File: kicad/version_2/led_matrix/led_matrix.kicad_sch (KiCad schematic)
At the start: 82 parts, among them Q1 IRF540N, Q2 IRF540N, Q3 IRF540N, Q4 IRF540N, Q5 IRF540N, Q6 IRF540N, Q7 IRF540N, Q9 IRF540N, SW1 SW_DIP_x01

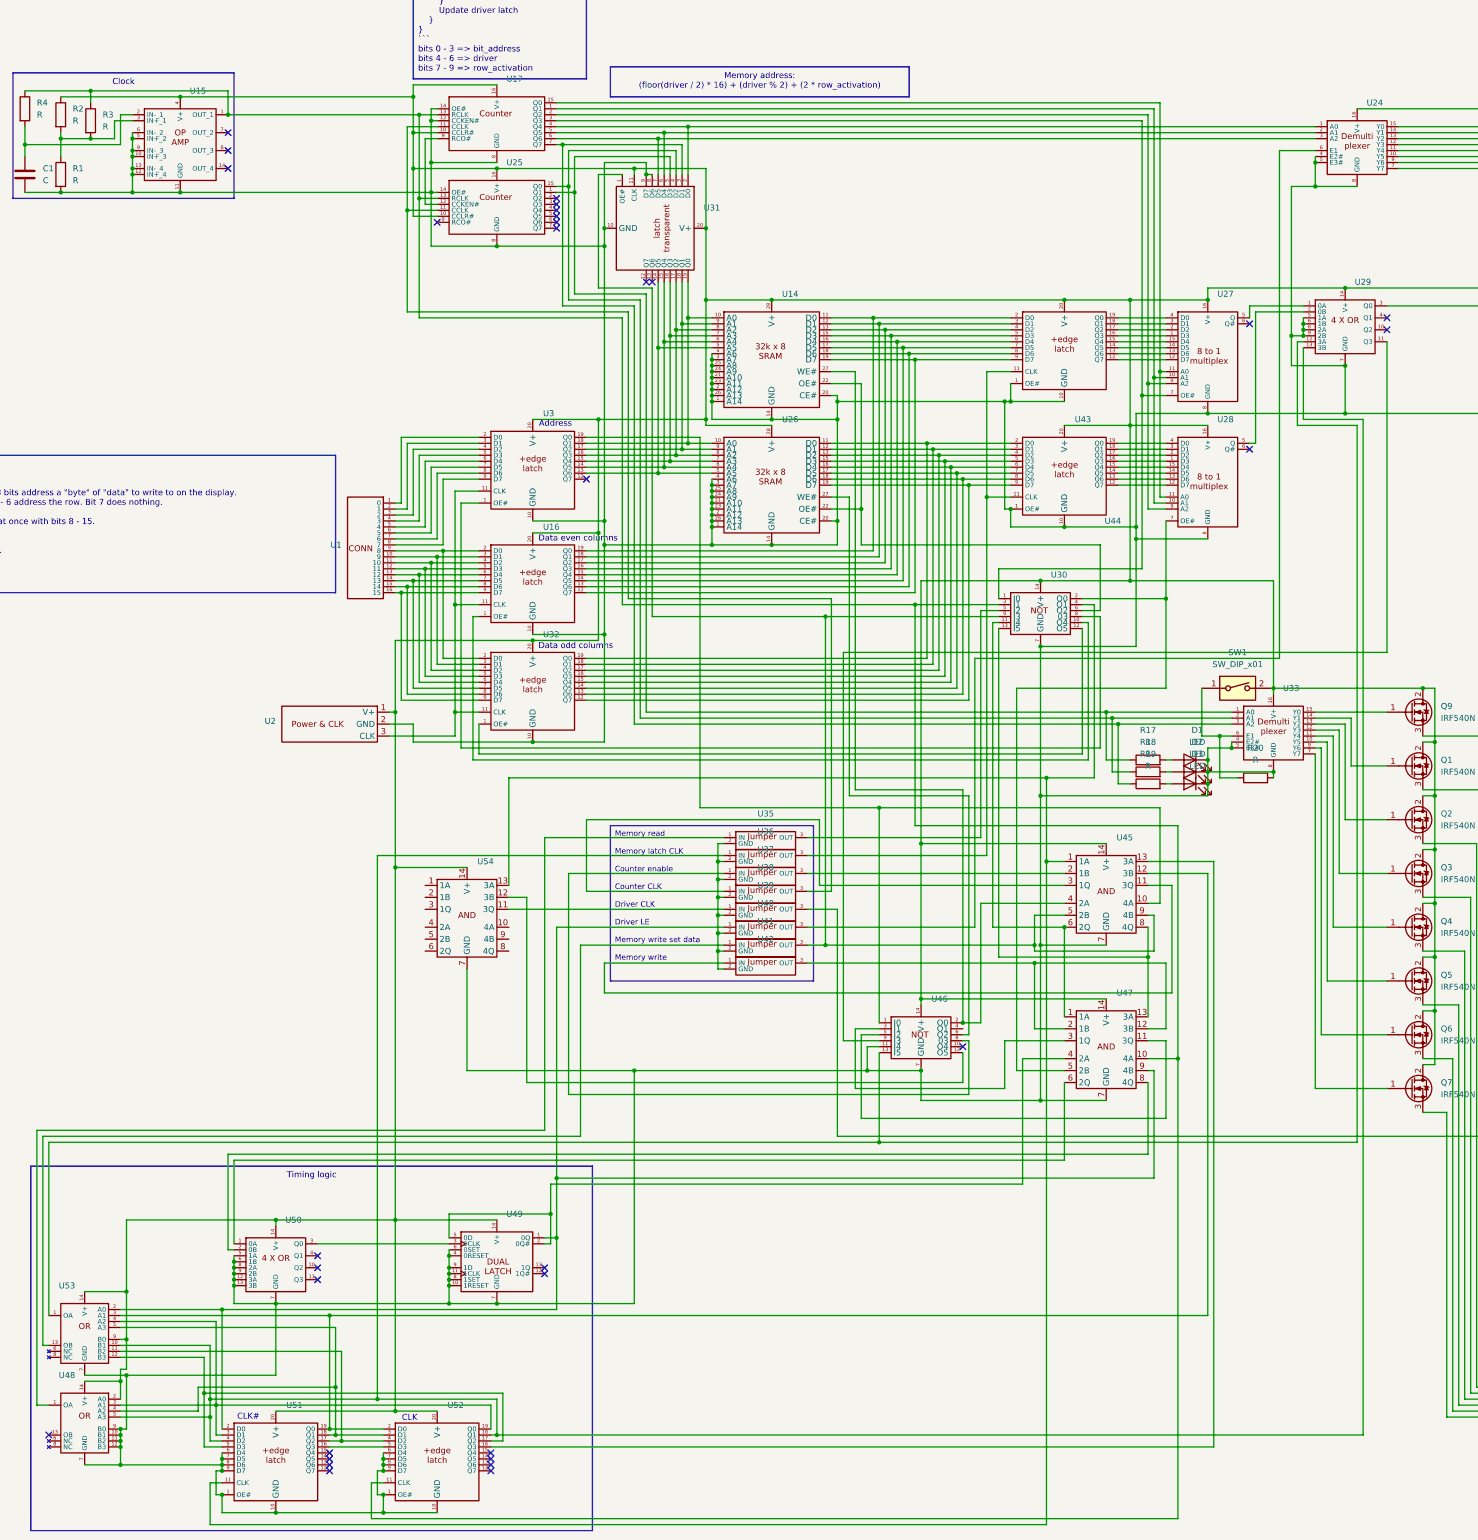
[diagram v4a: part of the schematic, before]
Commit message: LED matrix PCB done
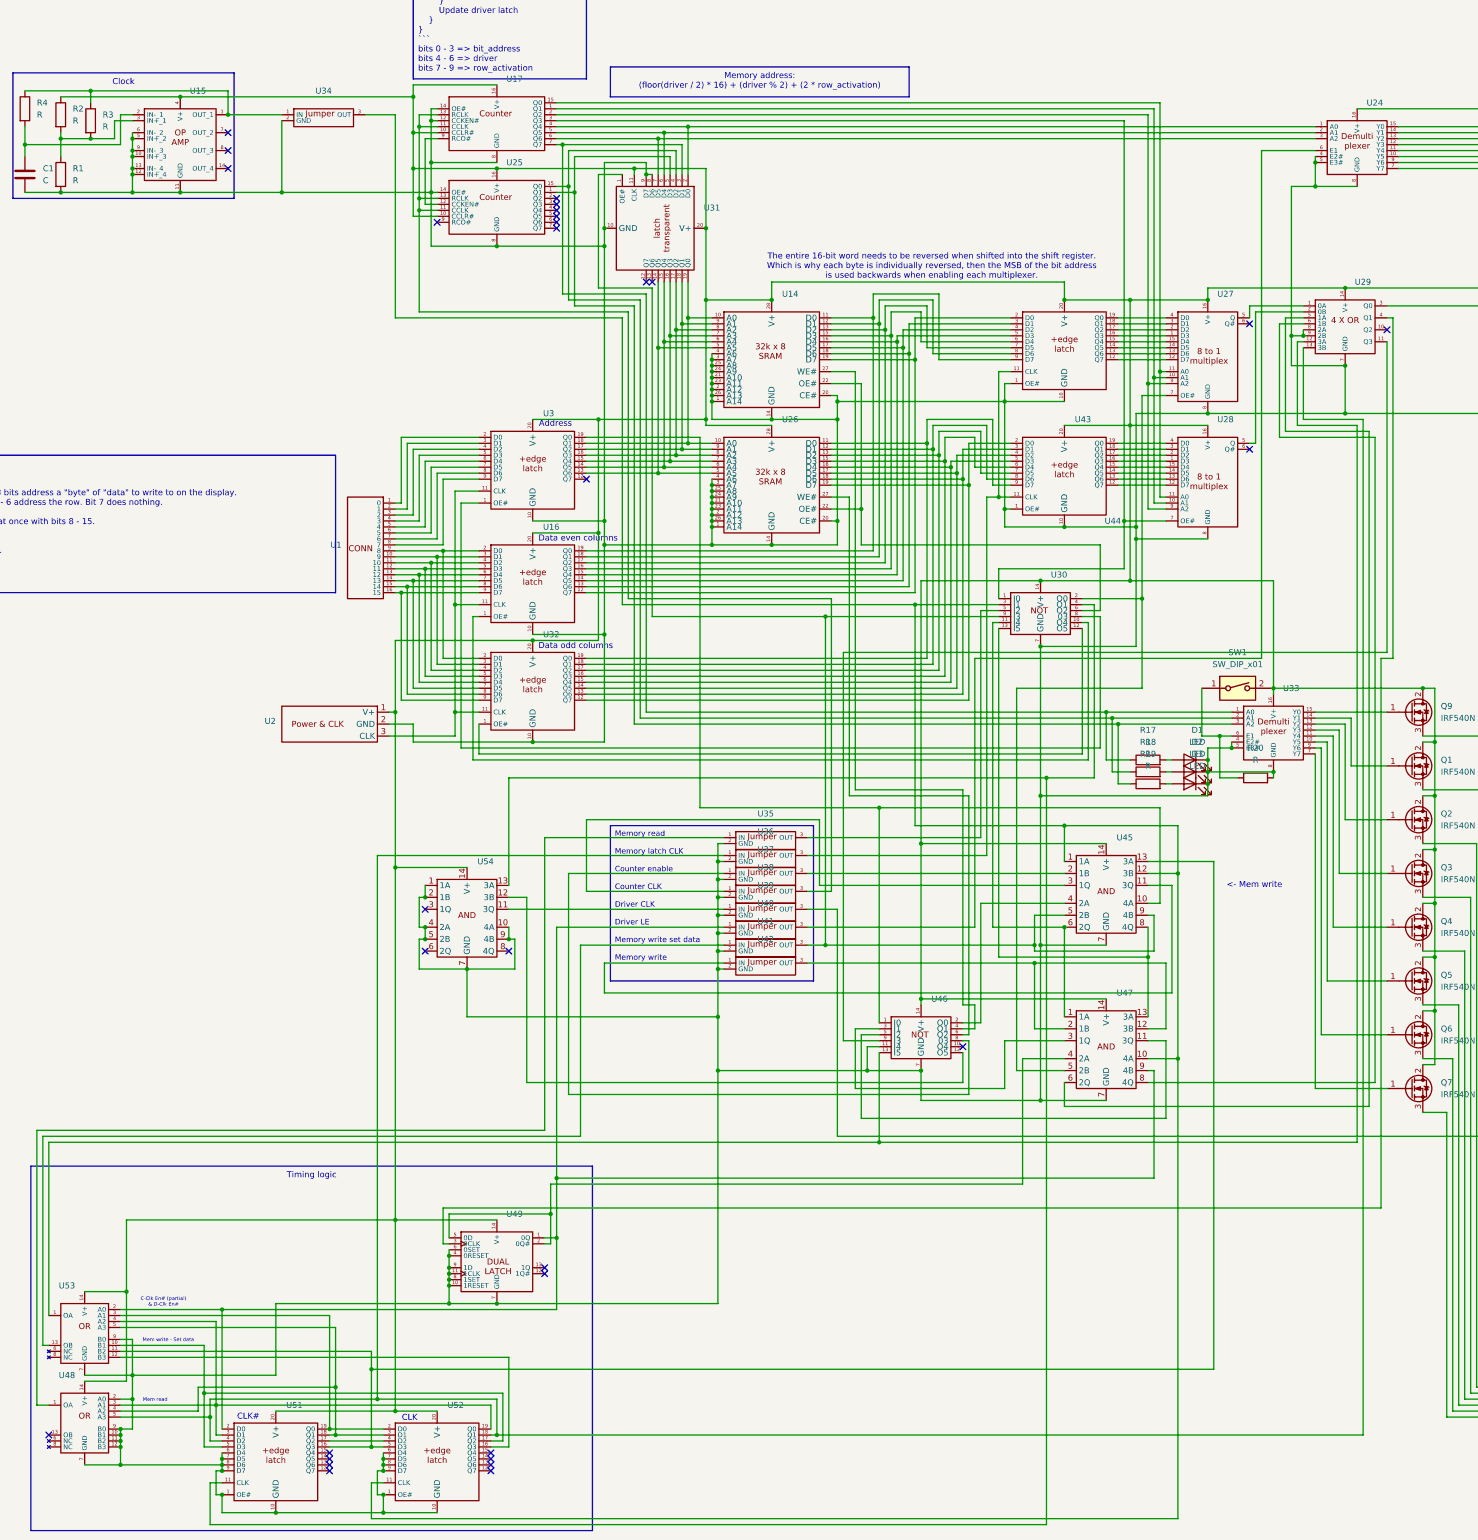
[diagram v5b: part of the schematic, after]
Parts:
- removed U50: ~, Package_DIP:DIP-14_W7.62mm, symbol custom_symbol_lib:quad_OR
- added U34: ~, custom_footprint_library:jumper, symbol custom_symbol_lib:jumper
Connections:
- net at U29.13 (3B), U36.1 (IN), U48.5 (A3)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: no longer U53.10 (B1)
- net at U51.17 (Q2), U52.4 (D2): no longer U53.11 (B2)
- net at U51.5 (D3), U52.17 (Q2): now also U53.10 (B1); no longer U53.12 (B3)
- net at Q1.2 (D), Q2.2 (D), Q3.2 (D)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: no longer U48.2 (A0), U53.9 (B0)
- net at U51.19 (Q0), U52.2 (D0), U53.3 (A1): no longer U45.12 (3B)
- net at C1.2, D1.1 (K), D2.1 (K)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: now also U35.2 (GND), U36.2 (GND), U37.2 (GND), U38.2 (GND), U39.2 (GND), U40.2 (GND), U41.2 (GND), U42.2 (GND), U48.2 (A0), U53.9 (B0), U54.1 (1A), U54.10 (4A), U54.2 (1B), U54.4 (2A), U54.5 (2B), U54.9 (4B), U34.2 (GND); no longer U29.5 (1A), U29.6 (1B)
- net at U17.3 (Q3), U30.1 (I0): now also U28.7 (OE#); no longer U27.7 (OE#)
- net at U30.2 (O0), U47.5 (2B): now also U27.7 (OE#); no longer U28.7 (OE#)
- net at U30.4 (O1), U51.11 (CLK), U54.13 (3A): no longer U45.1 (1A)
- net at U49.3 (0CLK): now also U29.4 (Q1)
- net at U45.13 (3A): now also U51.16 (Q3), U52.5 (D3), U53.11 (B2); no longer U52.16 (Q3)
- net at U45.4 (2A), U46.2 (O0): no longer U14.27 (WE#)
- net at U17.11 (CCLK), U25.11 (CCLK), U38.3 (OUT): now also U17.13 (RCLK), U25.13 (RCLK)
- net at U17.7 (Q7), U31.3 (D1): now also R17.1, U33.1 (A0); no longer R19.1, U33.3 (A2)
- net at U47.6 (2Q): now also U29.5 (1A)
- net at U47.8 (4Q): now also U29.6 (1B)
- net at U14.19 (D7), U16.12 (Q7): now also U44.2 (D0); no longer U44.9 (D7)
- net at U14.18 (D6), U16.13 (Q6): now also U44.3 (D1); no longer U44.8 (D6)
- net at U14.17 (D5), U16.14 (Q5): now also U44.4 (D2); no longer U44.7 (D5)
- net at U14.16 (D4), U16.15 (Q4): now also U44.5 (D3); no longer U44.6 (D4)
- net at U14.15 (D3), U16.16 (Q3): now also U44.6 (D4); no longer U44.5 (D3)
- net at U14.13 (D2), U16.17 (Q2): now also U44.7 (D5); no longer U44.4 (D2)
- net at U14.12 (D1), U16.18 (Q1): now also U44.8 (D6); no longer U44.3 (D1)
- net at U14.11 (D0), U16.19 (Q0): now also U44.9 (D7); no longer U44.2 (D0)
- net at U25.1 (Q1), U31.5 (D3): now also R19.1, U33.3 (A2); no longer R17.1, U33.1 (A0)
- net at U26.11 (D0), U32.19 (Q0): now also U43.9 (D7); no longer U43.2 (D0)
- net at U26.12 (D1), U32.18 (Q1): now also U43.8 (D6); no longer U43.3 (D1)
- net at U26.13 (D2), U32.17 (Q2): now also U43.7 (D5); no longer U43.4 (D2)
- net at U26.15 (D3), U32.16 (Q3): now also U43.6 (D4); no longer U43.5 (D3)
- net at U26.16 (D4), U32.15 (Q4): now also U43.5 (D3); no longer U43.6 (D4)
- net at U26.17 (D5), U32.14 (Q5): now also U43.4 (D2); no longer U43.7 (D5)
- net at U26.18 (D6), U32.13 (Q6): now also U43.3 (D1); no longer U43.8 (D6)
- net at U26.19 (D7), U32.12 (Q7): now also U43.2 (D0); no longer U43.9 (D7)
- net at U46.4 (O1): now also U14.27 (WE#)
- new net: U52.16 (Q3), U53.12 (B3)
- new net: U30.3 (I1), U34.3 (OUT), U45.1 (1A), U45.12 (3B), U47.10 (4A), U52.11 (CLK)
- new net: R3.1, R4.1, U15.1 (OUT_1), U34.1 (IN)
- no-connect marks 40 -> 39
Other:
- note added: "<- Mem write"
- note added: "C-Clk En# (partial) & D-Clk En#"
- note added: "Mem read"
- note added: "Mem write - Set data"
- note added: "The entire 16-bit word needs to be reversed when shifted into the shift register. Which is why each byte is individually reversed, then the MSB of the bit address is used backwards when enabling each multiplexer."

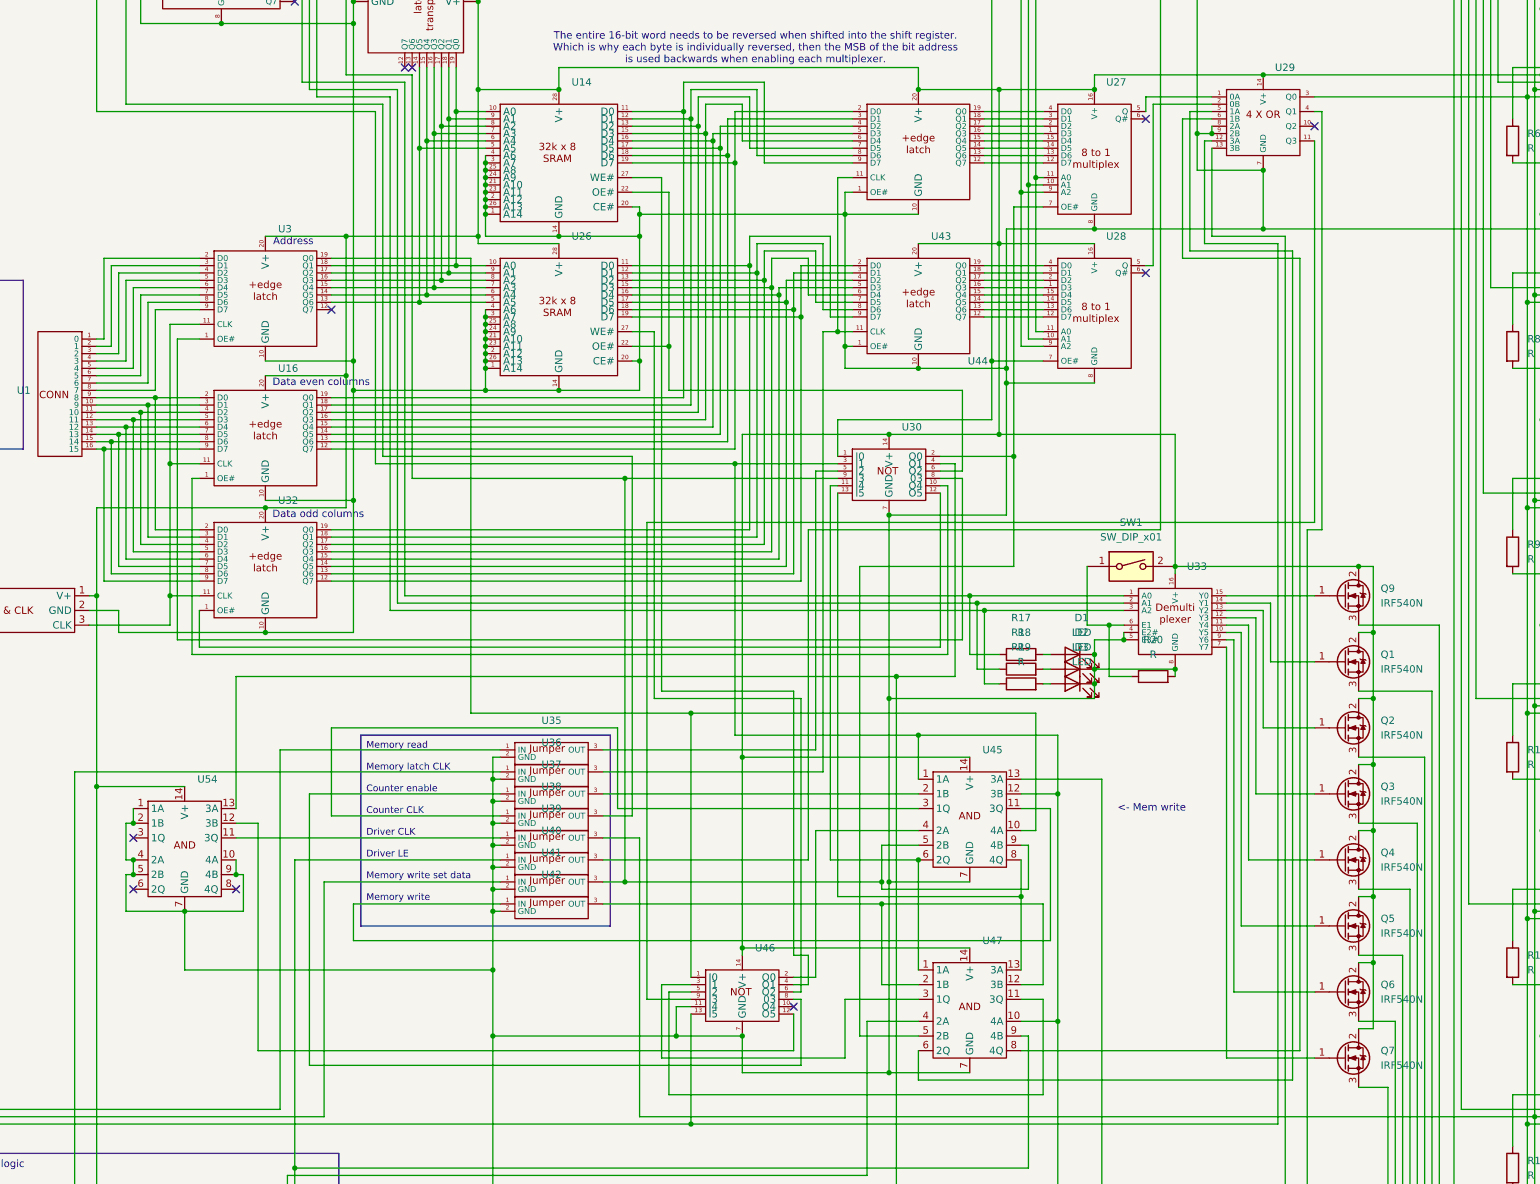
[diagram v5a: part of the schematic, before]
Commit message: Added failsafe to LED matrix and some other stuff
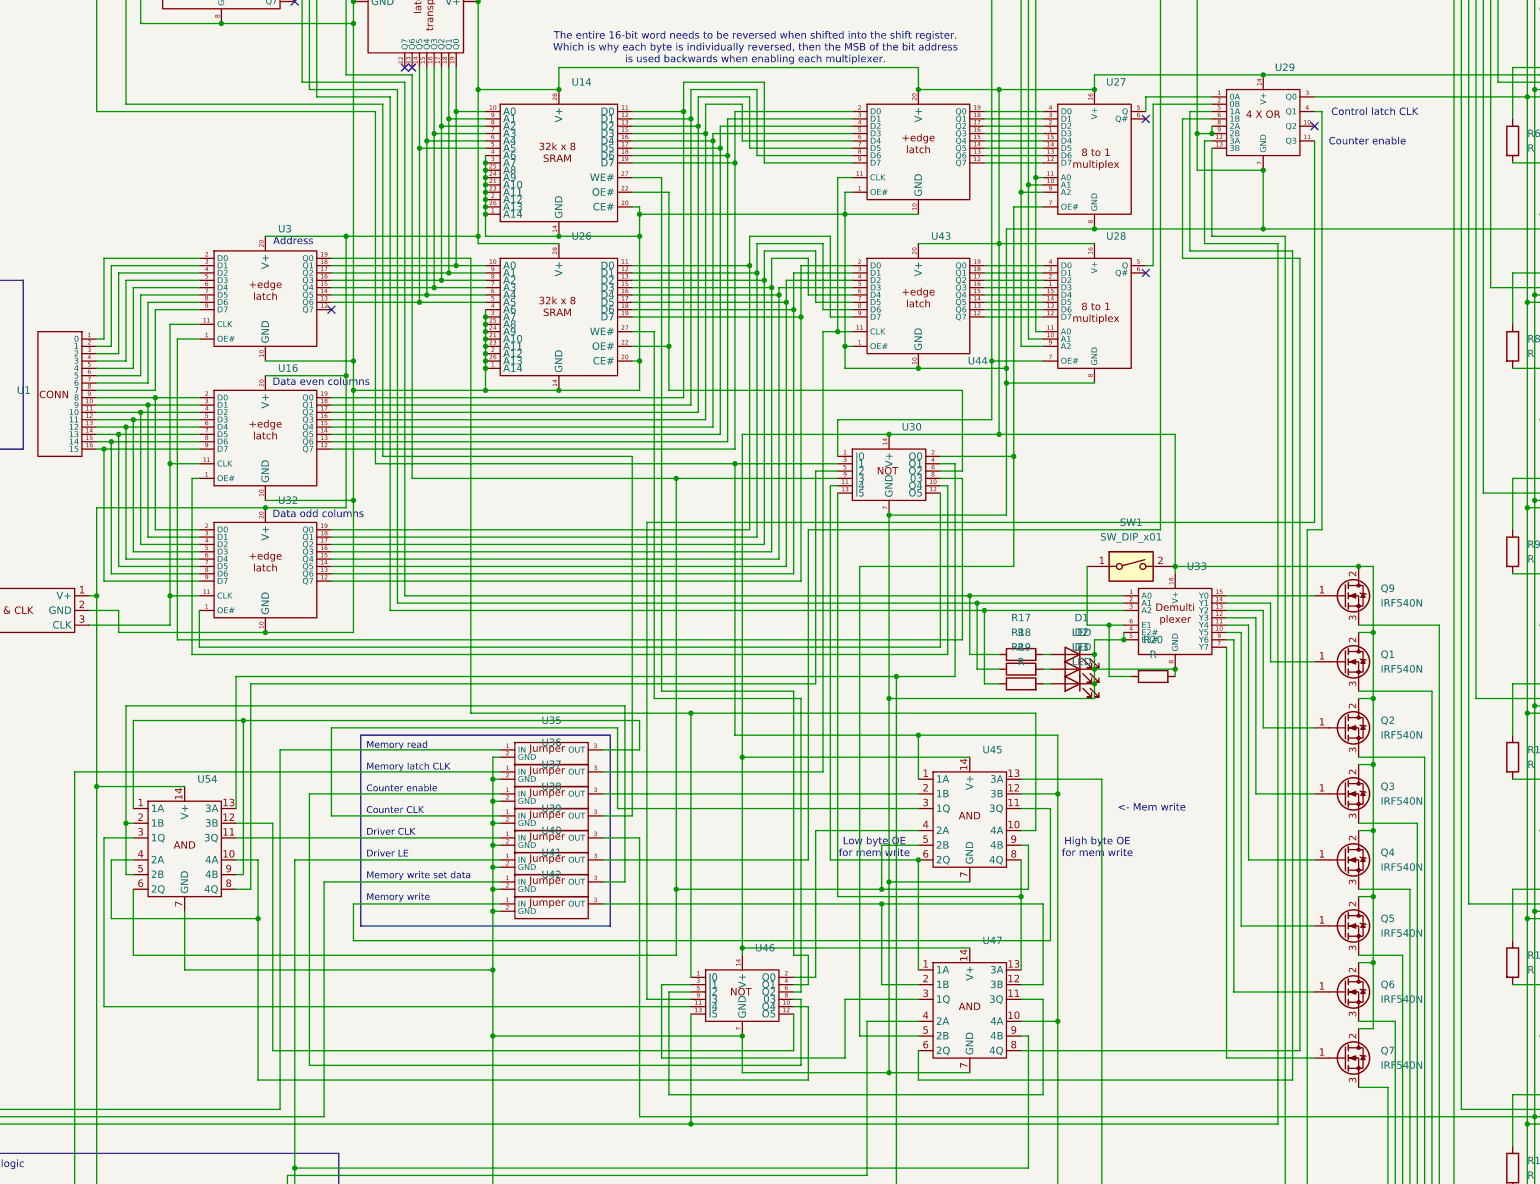
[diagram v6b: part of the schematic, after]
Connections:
- net at C1.2, D1.1 (K), D2.1 (K)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: no longer U46.11 (I4), U54.1 (1A), U54.10 (4A), U54.2 (1B), U54.4 (2A), U54.5 (2B), U54.9 (4B)
- net at U30.5 (I2): now also U54.8 (4Q); no longer U35.3 (OUT)
- net at U30.9 (I3), U31.1 (OE#), U45.5 (2B)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: now also U54.6 (2Q); no longer U41.3 (OUT)
- net at U54.3 (1Q): now also U46.11 (I4)
- net at U46.10 (O4): now also U54.10 (4A), U54.4 (2A)
- new net: U35.3 (OUT), U54.1 (1A), U54.9 (4B)
- new net: U41.3 (OUT), U54.2 (1B), U54.5 (2B)
- no-connect marks 39 -> 35
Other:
- note added: "Control latch CLK"
- note added: "Counter enable"
- note added: "High byte OE for mem write"
- note added: "Low byte OE for mem write"
